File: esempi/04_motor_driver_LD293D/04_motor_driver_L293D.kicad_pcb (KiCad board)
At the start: 2 copper layers, 38.1 x 38.1 mm, 20 parts, among them IC1 L293D, P1 MOTOR1_DIRECTION, P2 MOTOR1_ENABLE, P3 CONN_01X02, P4 MOTOR2_ENABLE, P5 CONN_01X02, P6 MOTOR2_DIRECTION, P7 CONN_01X01, P8 CONN_01X01, P9 CONN_01X01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

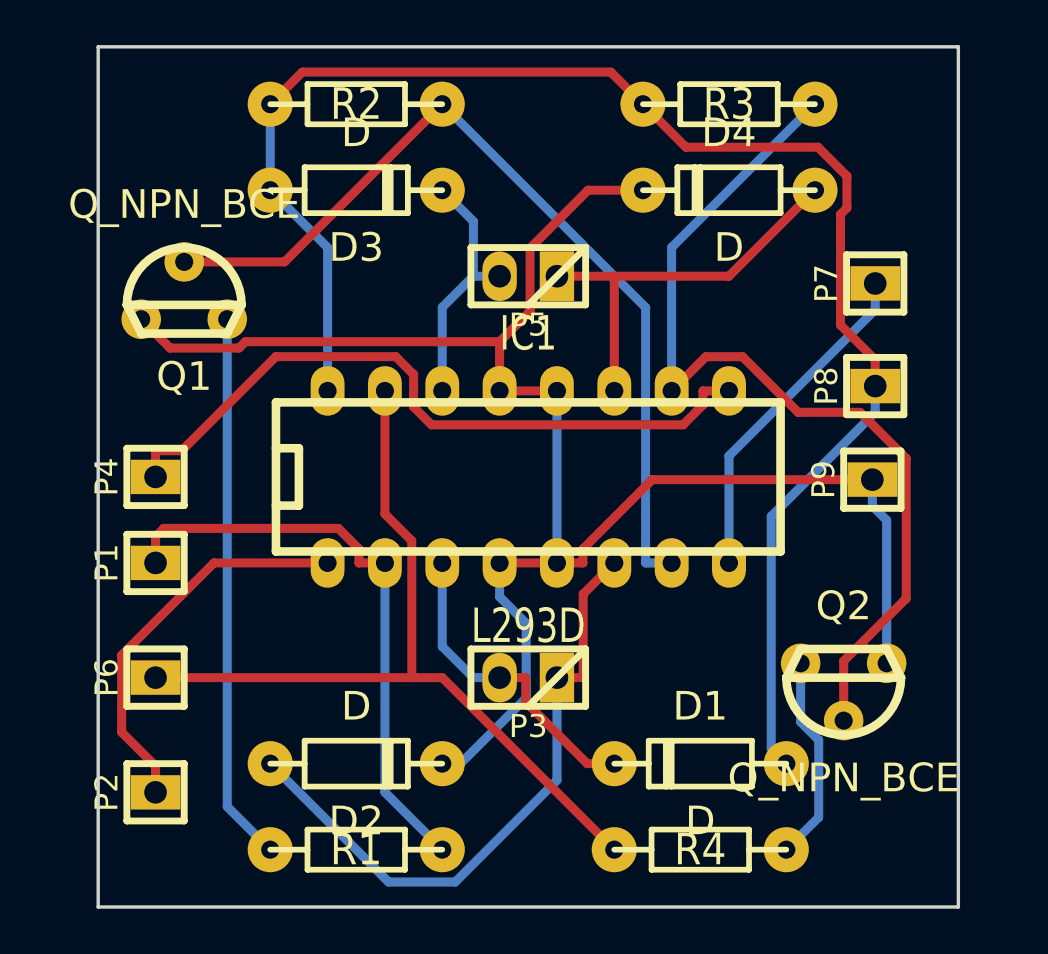
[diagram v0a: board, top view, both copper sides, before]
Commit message: sistemato circuito L293D aggiunti 2 diodi mancanti
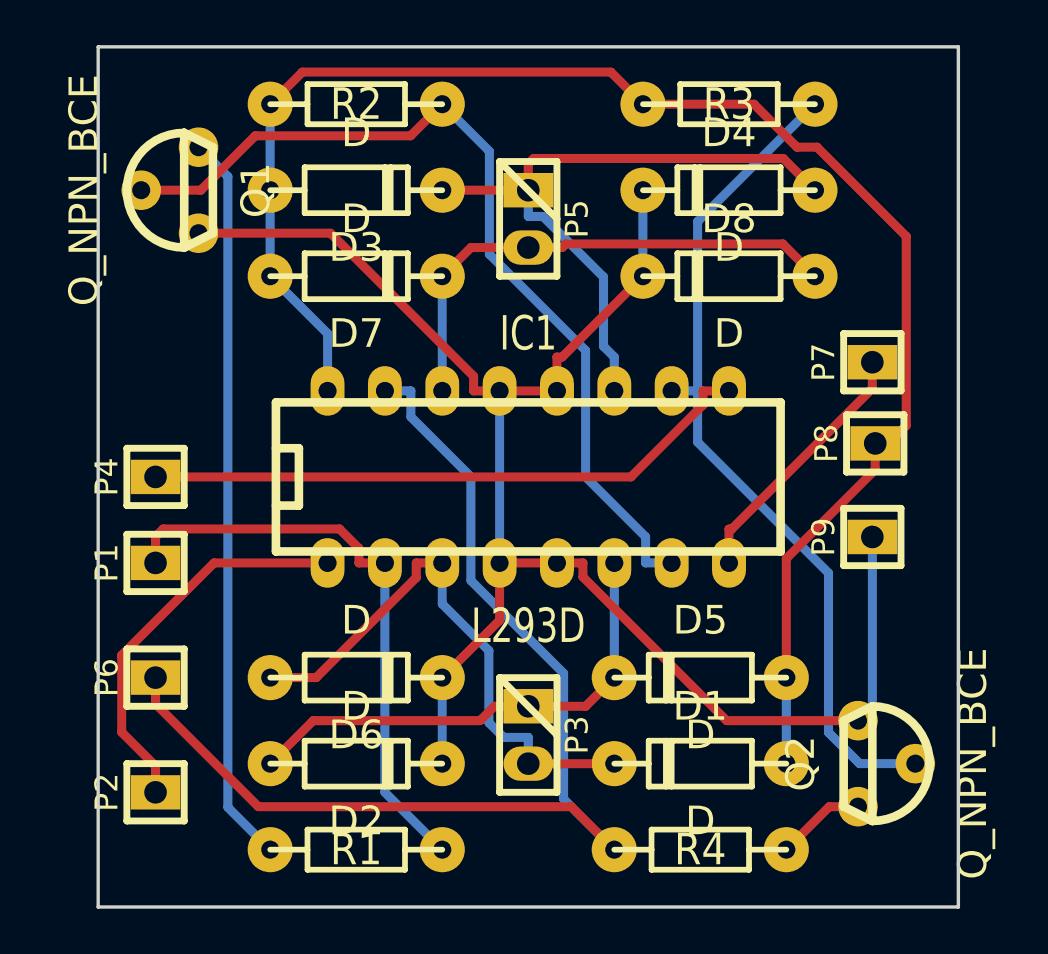
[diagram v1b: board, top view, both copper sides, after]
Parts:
- added D5: D, w_pth_diodes:diode_do35, F.Cu at (153.7, 104.1)
- added D6: D, w_pth_diodes:diode_do35, F.Cu at (138.4, 104.1)
- added D7: D, w_pth_diodes:diode_do35, F.Cu at (138.4, 86.4)
- added D8: D, w_pth_diodes:diode_do35, F.Cu at (154.9, 86.4)
- moved Q1 5.08 mm to (130.8, 82.5), turned to 90 degrees
- moved Q2 4.02 mm to (161.3, 108.0), turned to 270 degrees
- moved P7 3.49 mm to (161.3, 90.2)
- moved P3 2.54 mm to (146.1, 106.7), turned to 270 degrees
- moved P5 2.54 mm to (146.1, 83.8), turned to 270 degrees
- moved P9 2.54 mm to (161.3, 97.9)
- moved P8 2.54 mm to (161.4, 93.8)
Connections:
- D4 pad 1: Net-(D4-Pad1) -> Net-(D3-Pad2)
- IC1 pad 11: Net-(D4-Pad1) -> Net-(D3-Pad2)
- IC1 pad 14: Net-(D3-Pad2) -> Net-(D7-Pad2)
- P5 pad 1: Net-(D4-Pad1) -> Net-(D3-Pad2)
- P5 pad 2: Net-(D3-Pad2) -> Net-(D7-Pad2)
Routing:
- net Net-(D7-Pad2): track 0.00 -> 22.8 mm
- net Net-(D4-Pad1): track 18.1 -> 0.00 mm
- net Net-(D3-Pad2): track 11.2 -> 29.2 mm
- net Net-(IC1-Pad15): track 36.7 -> 49.4 mm
- net Net-(D1-Pad2): track 14.1 -> 25.0 mm
- net Net-(Q1-Pad1): track 24.3 -> 32.4 mm
- net Net-(D2-Pad1): track 28.1 -> 21.9 mm
- net Net-(Q2-Pad1): track 9.18 -> 3.96 mm
- net Net-(IC1-Pad9): track 31.4 -> 27.3 mm
- net VCC: track 15.1 -> 11.6 mm
- net Net-(IC1-Pad10): track 41.0 -> 38.0 mm
- net GND: track 77.8 -> 74.8 mm
- net +5V: track 70.8 -> 71.7 mm
- net Net-(IC1-Pad7): track 39.5 -> 40.1 mm

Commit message: Modifiche alla board per uso su motori recuperati da macchinetta caffe
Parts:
- added J1: Arduino_Nano_Header, w_conn_misc:arduino_nano_header, F.Cu at (114.3, 73.7)
- D1, D2, D3, D4, D5, D6, D7, D8: footprint w_pth_diodes:diode_do35 -> w_smd_diode:sod123; moved to B.Cu
- P1: value MOTOR1_DIRECTION -> OUT12; footprint w_pin_strip:pin_strip_1 -> w_pin_strip:pin_strip_2
- P2: value MOTOR1_ENABLE -> ALIM_HALL; footprint w_pin_strip:pin_strip_1 -> w_pin_strip:pin_strip_6
- P3: value CONN_01X02 -> MOTOR_CTR; footprint w_pin_strip:pin_strip_2 -> w_pin_strip:pin_strip_4
- P4: value MOTOR2_ENABLE -> OUT34; footprint w_pin_strip:pin_strip_1 -> w_pin_strip:pin_strip_2
- P5: value CONN_01X02 -> HALL_01; footprint w_pin_strip:pin_strip_2 -> w_pin_strip:pin_strip_2mm_3
- P6: value MOTOR2_DIRECTION -> HOLE1; footprint w_pin_strip:pin_strip_1 -> w_details:hole_3mm5
- P7: value CONN_01X01 -> HOLE2; footprint w_pin_strip:pin_strip_1 -> w_details:hole_3mm5
- P8: value CONN_01X01 -> HALL_02; footprint w_pin_strip:pin_strip_1 -> w_pin_strip:pin_strip_2mm_3
- P9: value CONN_01X01 -> ING5V; footprint w_pin_strip:pin_strip_1 -> w_pin_strip:pin_strip_2
- R1, R2, R3, R4: footprint w_pth_resistors:RC03 -> w_smd_resistors:r_0805; moved to B.Cu
- moved Q2 69.1 mm to (101.0, 74.3), turned to 90 degrees
- moved P9 67.3 mm to (95.2, 85.1), turned to 0 degrees
- moved R4 66.3 mm to (102.2, 69.8)
- moved D5 53.4 mm to (109.9, 73.7), turned to 0 degrees
- moved P8 45.3 mm to (116.8, 85.7), turned to 180 degrees
- moved D6 44.7 mm to (101.6, 78.7), turned to 180 degrees
- moved P6 44.6 mm to (95.2, 75.6), turned to 0 degrees
- moved P4 43.7 mm to (94.0, 69.8)
- moved D2 43.5 mm to (147.3, 65.4), turned to 180 degrees
- moved D8 39.0 mm to (118.1, 73.7)
- moved IC1 37.4 mm to (115.6, 73.7)
- moved P1 34.3 mm to (148.6, 70.5), turned to 270 degrees
- moved R1 34.2 mm to (132.1, 78.1), turned to 0 degrees
- moved P2 32.3 mm to (140.3, 78.7)
- moved D1 31.0 mm to (132.1, 85.7), turned to 0 degrees
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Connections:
- D2 pad 1: Net-(D2-Pad1) -> Net-(D1-Pad2)
- D5 pad 2: Net-(D2-Pad1) -> Net-(D5-Pad2)
- D6 pad 1: Net-(D1-Pad2) -> Net-(D5-Pad2)
- IC1 pad 1: Net-(IC1-Pad1) -> 1,2EN
- IC1 pad 11: Net-(D3-Pad2) -> Net-(D7-Pad2)
- IC1 pad 14: Net-(D7-Pad2) -> Net-(D5-Pad2)
- IC1 pad 15: Net-(IC1-Pad15) -> 3,4DIR
- IC1 pad 2: Net-(IC1-Pad2) -> 1,2DIR
- IC1 pad 3: Net-(D1-Pad2) -> Net-(D3-Pad2)
- IC1 pad 6: Net-(D2-Pad1) -> Net-(D1-Pad2)
- IC1 pad 9: Net-(IC1-Pad9) -> 3,4EN
- P1 pad 1: Net-(IC1-Pad2) -> Net-(D1-Pad2)
- P2 pad 1: Net-(IC1-Pad1) -> GND
- P3 pad 1: Net-(D2-Pad1) -> 3,4DIR
- P3 pad 2: Net-(D1-Pad2) -> 1,2DIR
- P4 pad 1: Net-(IC1-Pad9) -> Net-(D7-Pad2)
- P5 pad 1: Net-(D3-Pad2) -> +5V
- P5 pad 2: Net-(D7-Pad2) -> GND
- P6 pad 1: Net-(IC1-Pad15) -> (no net)
- P7 pad 1: VCC -> (no net)
- R1 pad 1: Net-(IC1-Pad2) -> 1,2DIR
- R4 pad 1: Net-(IC1-Pad15) -> 3,4DIR
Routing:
- net 3,4DIR: track 0.00 -> 87.0 mm
- net GND: track 74.8 -> 135.9 mm
- net 1,2DIR: track 0.00 -> 58.7 mm, vias 0 -> 1
- net 1,2EN: track 0.00 -> 56.7 mm
- net Net-(D3-Pad2): track 29.2 -> 82.3 mm, vias 0 -> 1
- net 3,4EN: track 0.00 -> 52.9 mm
- net Net-(IC1-Pad15): track 49.4 -> 0.00 mm
- net Net-(J1-Pad20): track 0.00 -> 46.5 mm
- net Net-(J1-Pad19): track 0.00 -> 41.1 mm
- net Net-(D5-Pad2): track 0.00 -> 34.5 mm
- net +5V: track 71.7 -> 102.4 mm
- net Net-(D1-Pad2): track 25.0 -> 55.1 mm, vias 0 -> 1
- net Net-(Q1-Pad1): track 32.4 -> 2.67 mm
- net Net-(IC1-Pad9): track 27.3 -> 0.00 mm
- net Net-(IC1-Pad2): track 26.2 -> 0.00 mm
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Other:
- board size 38.1 x 38.1 mm -> 59.7 x 24.1 mm
- net class Default: trace_width 0.4 -> 0.25; via_dia 1.2 -> 0.6; via_drill 0.8 -> 0.4
- net class Motor added: clearance 0.3, trace_width 0.5, via_dia 0.6, via_drill 0.4

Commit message: Aggiunti connettori e corrette connessioni a pin pwm
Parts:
- added P10: SER, w_pin_strip:pin_strip_3, F.Cu at (102.9, 85.1)
- added P11: EXT_MOT, w_pin_strip:pin_strip_5, F.Cu at (144.8, 80.0)
- P3: value MOTOR_CTR -> CONN_MOT1; footprint w_pin_strip:pin_strip_4 -> w_pin_strip:pin_strip_5
- moved D4 3.24 mm to (145.4, 69.8)
- moved P3 1.27 mm to (148.6, 80.0)
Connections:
- J1 pad 1: (no net) -> Net-(J1-Pad1)
- J1 pad 10: 3,4EN -> Net-(J1-Pad10)
- J1 pad 11: (no net) -> Net-(J1-Pad11)
- J1 pad 12: (no net) -> 1,2EN
- J1 pad 13: (no net) -> 3,4EN
- J1 pad 14: (no net) -> Net-(J1-Pad14)
- J1 pad 2: (no net) -> Net-(J1-Pad2)
- J1 pad 4: (no net) -> Net-(J1-Pad4)
- J1 pad 6: (no net) -> Net-(J1-Pad6)
- J1 pad 9: 1,2EN -> (no net)
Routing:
- net GND: track 135.9 -> 0.00 mm
- net +5V: track 102.4 -> 0.00 mm
- net 3,4DIR: track 87.0 -> 0.00 mm
- net Net-(D3-Pad2): track 82.3 -> 0.00 mm, vias 1 -> 0
- net 1,2DIR: track 58.7 -> 0.00 mm, vias 1 -> 0
- net 1,2EN: track 56.7 -> 0.00 mm
- net Net-(D1-Pad2): track 55.1 -> 0.00 mm, vias 1 -> 0
- net 3,4EN: track 52.9 -> 0.00 mm
- net Net-(J1-Pad20): track 46.5 -> 0.00 mm
- net Net-(J1-Pad19): track 41.1 -> 0.00 mm
- net Net-(IC1-Pad10): track 39.9 -> 0.00 mm
- net Net-(D5-Pad2): track 34.5 -> 0.00 mm
- net Net-(D7-Pad2): track 34.0 -> 0.00 mm
- net Net-(IC1-Pad7): track 18.7 -> 0.00 mm
- net VCC: track 16.9 -> 0.00 mm, vias 1 -> 0
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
